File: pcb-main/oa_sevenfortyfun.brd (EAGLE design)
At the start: 88.9 x 71.1 mm, 46 parts, among them J1 1X01-TERM, J2 1X01-TERM, J3 1X01-TERM, J4 1X01-TERM, J5 1X01-TERM, J6 1X01-TERM, J7 1X01-TERM, J8 1X01-TERM, J9 2X04SHR, Q1 2N3904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

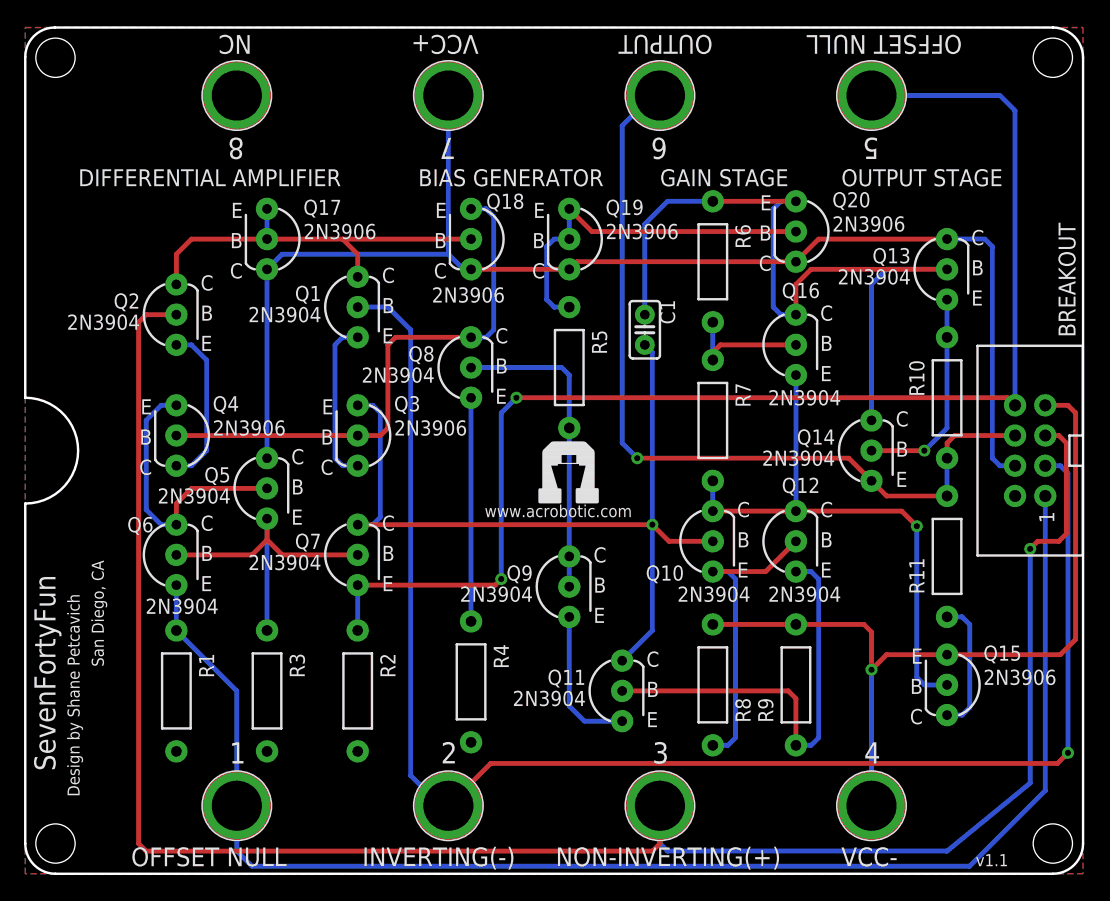
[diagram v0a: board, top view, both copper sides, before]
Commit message: matching functional blocks to v1.0
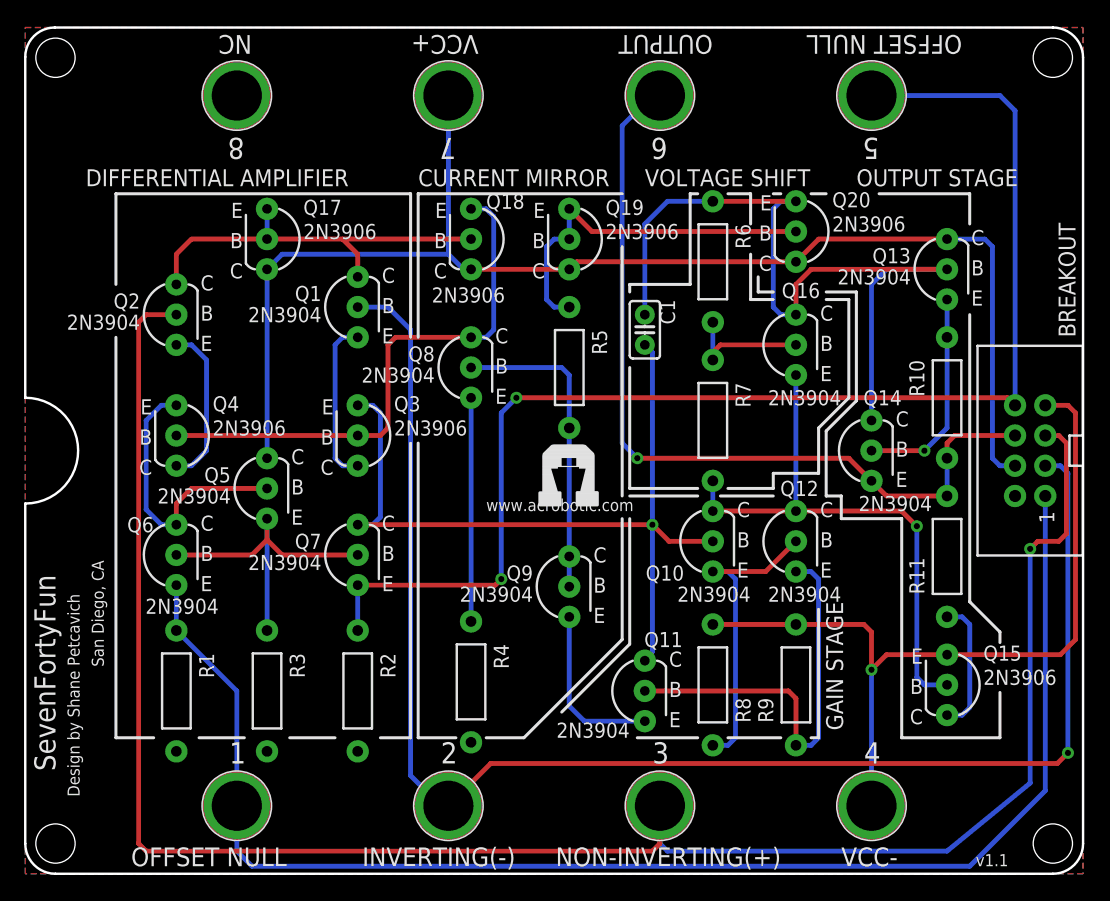
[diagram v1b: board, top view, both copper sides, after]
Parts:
- moved Q11 1.91 mm to (52.1, 15.4)
- moved U$3 0.25 mm to (45.7, 33.0)
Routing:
- net VCC-: track 80.7 -> 82.6 mm
- net N$21: track 36.5 -> 34.6 mm
- net N$5: track 71.4 -> 70.6 mm
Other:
- board text added: "CURRENT MIRROR"
- board text added: "VOLTAGE SHIFT"
- board text removed: "BIAS GENERATOR"
